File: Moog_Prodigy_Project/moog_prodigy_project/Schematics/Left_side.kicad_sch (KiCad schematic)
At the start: 70 parts, among them Q1 BC549, Q3 BC549, SW1 Switch_4x4, SW2 Switch_4x4, U2 NE5532, U2A1 OPA134, U2B1 OPA134, U3 NE5532, U4 NE5532, U5 LT1011CN8

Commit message: MOOG prodigy final 03.07.2026
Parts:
- R13: value 4K75 -> 4K75 1%
- R18: value 18K2 -> 18K2 1%
- R29: value 51M -> 51M 1%
- R3: value 63K4 -> 63K4 1%
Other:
- note added: "NAPOMENA 1 Kondenzatori: C37,C38,C39,C49,C41,C42, C43,C44,C45,C46,C47,C48 su vrednosti 100n i oni su kvalitetniji"
- note added: "NAPOMENA 2 Otpornici cija je vrednost: 63K4, 18K2, 4K75, 6K81, 51M, 2M4 su otpornici iz E96 serije (1%) Ostali orpotnici su iz serije E24 (5%)"
- note added: "Talasni oblik signala po promeni položaja preklopnika: Rampa - levi položaj Trougao - srednji položaj Četvrtke - desni položaj"
- note removed: "NAPOMENA Kondenzatori: C37,C38,C39,C49,C41,C42, C43,C44,C45,C46,C47,C48 su vrednosti 100n i oni su kvalitetniji"
- note removed: "Talasni oblik signala po promeni položaja preklopnika: Rampa - krajnji levi položaj Trougao - srednji položaj Četvrtke - krajnji desni položaj"
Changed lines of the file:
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@@
 		(comment 4 "Jovan Mastelica E1 105/2023")
 	)
+	(text "NAPOMENA 2\nOtpornici cija je vrednost:\n63K4, 18K2, 4K75, 6K81, 51M, 2M4\nsu otpornici iz E96 serije (1%)\nOstali orpotnici su iz serije E24 (5%)"
+		(exclude_from_sim no)
+		(at 217.678 160.02 0)
+		(effects
+			(font
+				(size 1.27 1.27)
+				(thickness 0.254)
+				(bold yes)
+			)
+			(justify left)
+		)
+	)
 	(text "OSC 1 CHIP \nTEMP TRIM"
 		(exclude_from_sim no)
@@
 		)
 	)
-	(text "Talasni oblik signala po promeni položaja preklopnika:\nRampa - krajnji levi položaj\nTrougao - srednji položaj\nČetvrtke - krajnji desni položaj\n"
+	(text "Talasni oblik signala po promeni položaja preklopnika:\nRampa -  levi položaj\nTrougao - srednji položaj\nČetvrtke - desni položaj\n"
 		(exclude_from_sim no)
-		(at 215.9 28.956 0)
+		(at 218.694 28.702 0)
 		(effects
 			(font
 				(size 1.27 1.27)
+				(thickness 0.254)
+				(bold yes)
 			)
 			(justify left)
@@
 		)
 	)
-	(text "NAPOMENA\nKondenzatori:\nC37,C38,C39,C49,C41,C42,\nC43,C44,C45,C46,C47,C48\nsu vrednosti 100n i oni su kvalitetniji"
+	(text "NAPOMENA 1\nKondenzatori:\nC37,C38,C39,C49,C41,C42,\nC43,C44,C45,C46,C47,C48\nsu vrednosti 100n i oni su kvalitetniji"
 		(exclude_from_sim no)
 		(at 177.038 160.274 0)
@@
 		(dnp no)
 		(property "Reference" "R3"
-			(at 28.702 153.162 0)
+			(at 27.178 152.908 0)
 			(effects
 				(font
@@
 			)
 		)
-		(property "Value" "63K4"
-			(at 27.432 155.448 0)
+		(property "Value" "63K4 1%"
+			(at 24.13 155.194 0)
 			(effects
 				(font
@@
 			)
 		)
-		(property "Value" "18K2"
+		(property "Value" "18K2 1%"
 			(at 147.574 125.73 0)
 			(effects
@@
 			)
 		)
-		(property "Value" "4K75"
+		(property "Value" "4K75 1%"
 			(at 109.474 68.834 90)
 			(effects
@@
 			)
 		)
-		(property "Value" "51M"
+		(property "Value" "51M 1%"
 			(at 251.46 134.874 90)
 			(effects

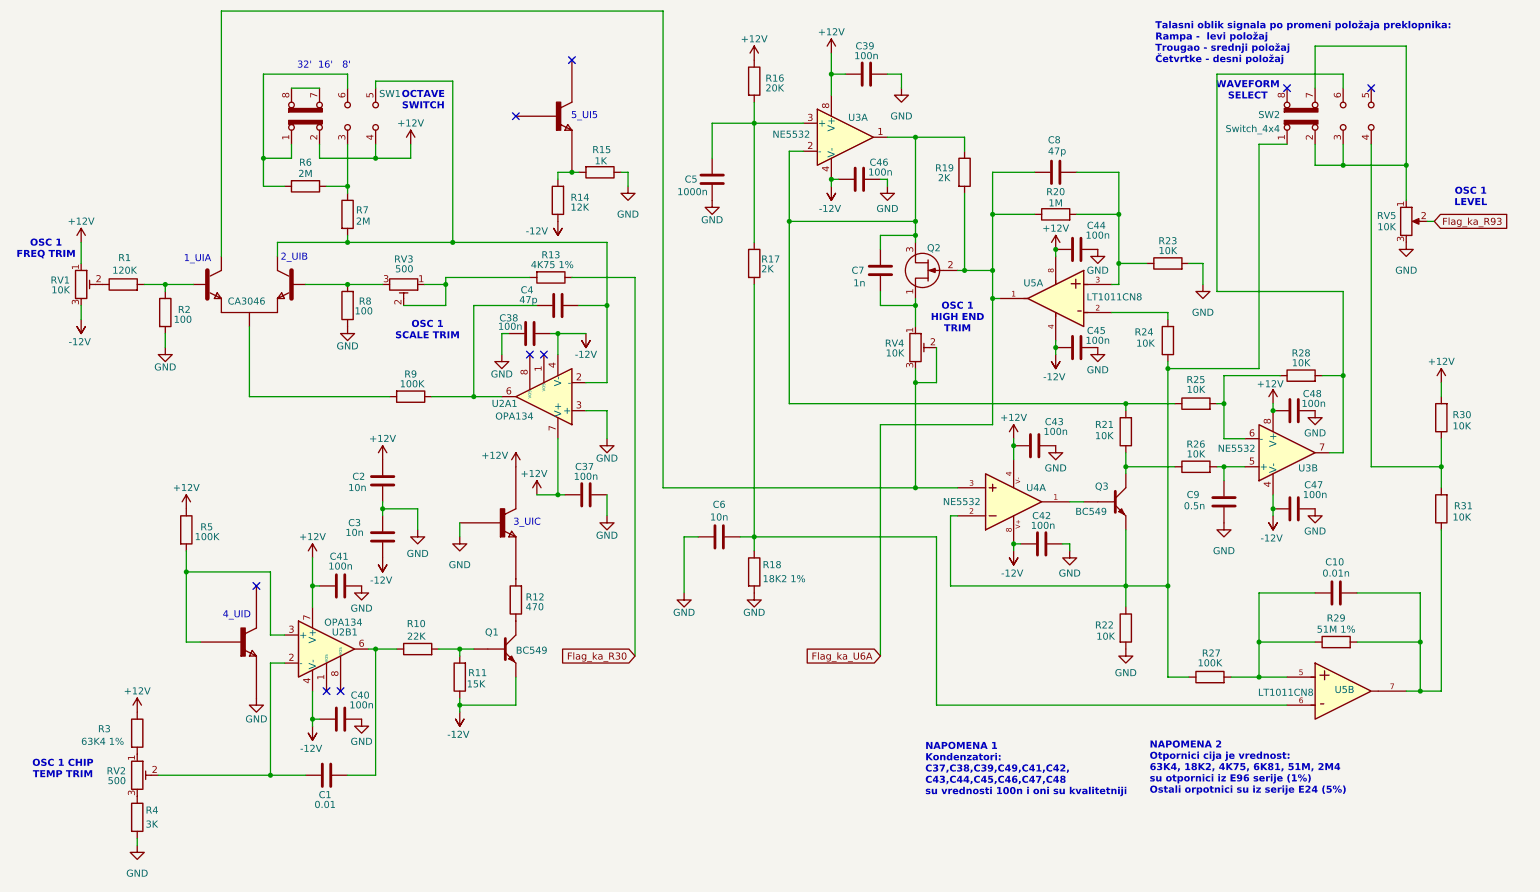
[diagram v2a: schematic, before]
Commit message: Moog prodigy fix 3
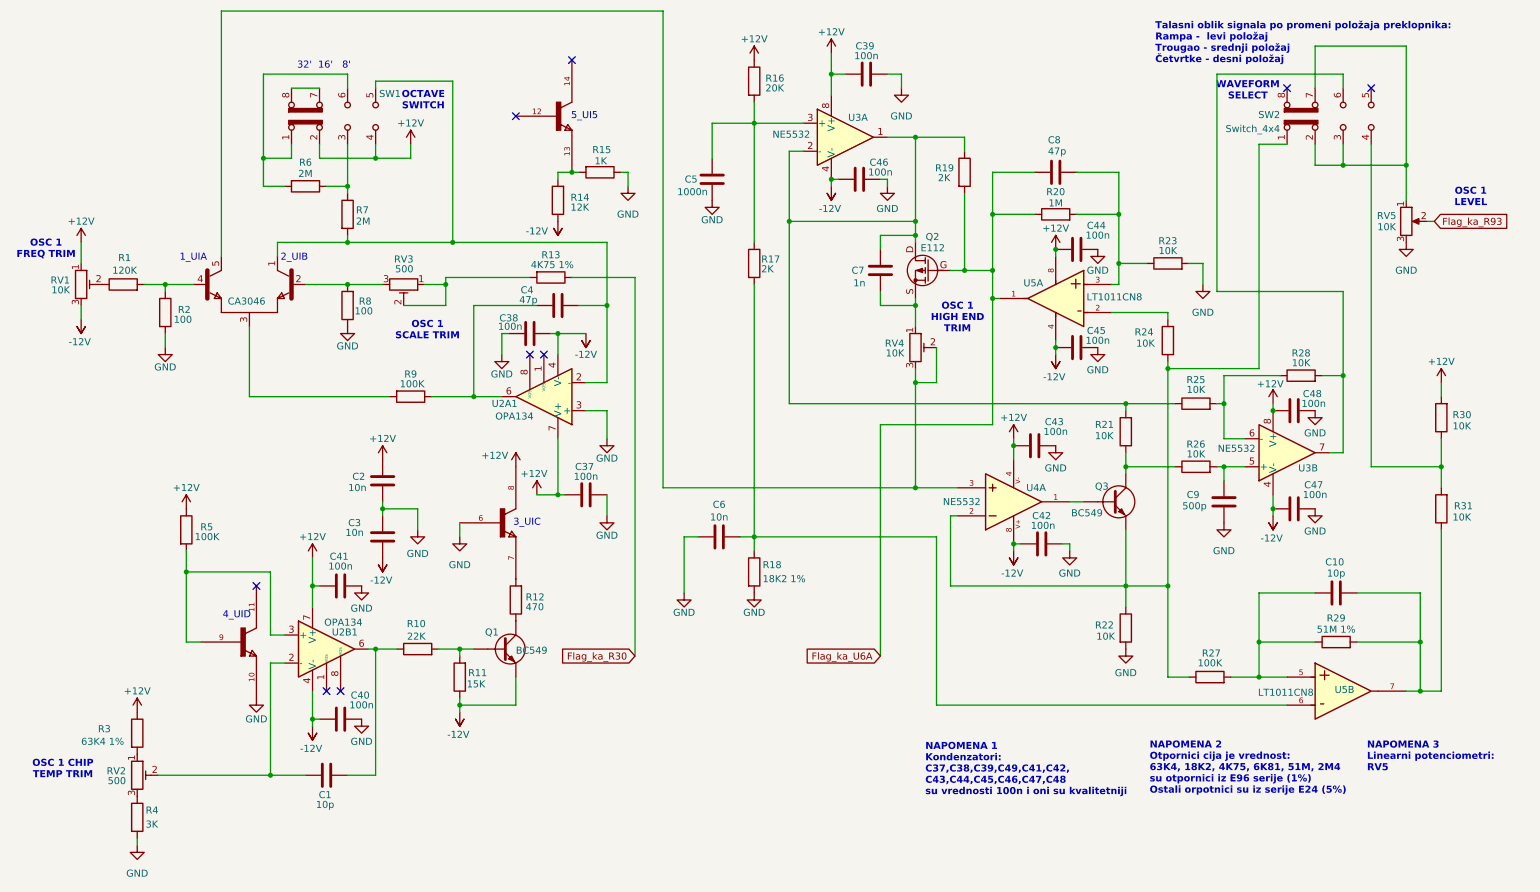
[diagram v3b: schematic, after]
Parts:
- C1: value 0.01 -> 10p
- C10: value 0.01n -> 10p
- C9: value 0.5n -> 500p
- Q2: value ~ -> E112
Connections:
- net +12V: now also CA3046.8; no longer CA3046.
- net Flag_ka_U6A: now also Q2.G; no longer Q2.2
- net GND: now also CA3046.10, CA3046.6; no longer CA3046.
- net at R1.2, R2.1: now also CA3046.4; no longer CA3046.
- net at C7.1, RV4.1: now also Q2.S; no longer Q2.1
- net at RV4.2, RV4.3, U4.3: now also CA3046.5; no longer CA3046.
- net at C4.2, R7.2, SW1.5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: now also CA3046.1; no longer CA3046.
- net at C7.2, R19.1, R21.2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: now also Q2.D; no longer Q2.3
- net at R8.2, RV3.3: now also CA3046.2; no longer CA3046.
- net at R12.2: now also CA3046.7; no longer CA3046.
- net at R9.2: now also CA3046.3; no longer CA3046.
- net at R14.2, R15.2: now also CA3046.13; no longer CA3046.
- net at R5.2, U2B1.3 (+): now also CA3046.9; no longer CA3046.
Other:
- note added: "NAPOMENA 3 Linearni potenciometri: RV5"
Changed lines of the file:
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@@
 		)
 	)
+	(text "NAPOMENA 3\nLinearni potenciometri:\nRV5"
+		(exclude_from_sim no)
+		(at 257.048 157.988 0)
+		(effects
+			(font
+				(size 1.27 1.27)
+				(thickness 0.254)
+				(bold yes)
+			)
+			(justify left)
+		)
+	)
 	(text "2_UIB"
 		(exclude_from_sim no)
@@
 	(text "1_UIA"
 		(exclude_from_sim no)
-		(at 45.212 67.818 0)
+		(at 44.45 67.564 0)
 		(effects
 			(font
@@
 	(wire
 		(pts
+			(xy 181.61 69.85) (xy 184.15 69.85)
+		)
+		(stroke
+			(width 0)
+			(type default)
+		)
+	)
+	(wire
+		(pts
 			(xy 78.74 111.76) (xy 78.74 113.03)
 		)
@@
 	(wire
 		(pts
-			(xy 182.88 69.85) (xy 184.15 69.85)
-		)
-		(stroke
-			(width 0)
-			(type default)
-		)
-	)
-	(wire
-		(pts
 			(xy 266.7 137.16) (xy 266.7 146.05)
 		)
@@
 	(symbol
 		(lib_id "Transistor_FET:BF256C")
-		(at 180.34 67.31 180)
+		(at 179.07 69.85 180)
 		(unit 1)
 		(exclude_from_sim no)
@@
 		(dnp no)
 		(property "Reference" "Q2"
-			(at 179.832 65.786 0)
+			(at 179.578 63.754 0)
 			(effects
 				(font
@@
 			)
 		)
-		(property "Value" "~"
-			(at 173.99 71.1199 0)
+		(property "Value" "E112"
+			(at 180.594 65.786 0)
 			(effects
 				(font
@@
 				)
 				(justify left)
-				(hide yes)
 			)
 		)
 		(property "Footprint" "Package_TO_SOT_THT:TO-92_Inline"
-			(at 180.34 67.31 0)
+			(at 179.07 69.85 0)
 			(effects
 				(font
@@
 		)
 		(property "Datasheet" ""
-			(at 180.34 67.31 0)
+			(at 179.07 69.85 0)
 			(effects
 				(font
@@
 		)
 		(property "Description" ""
-			(at 180.34 67.31 0)
+			(at 179.07 69.85 0)
 			(effects
 				(font
@@
 			)
 		)
-		(pin "1"
+		(pin "D"
 		)
-		(pin "3"
+		(pin "G"
 		)
-		(pin "2"
+		(pin "S"
 		)
 		(instances
@@
 			)
 		)
-		(property "Value" "0.01"
+		(property "Value" "10p"
 			(at 68.326 166.624 90)
 			(effects
@@
 			)
 		)
-		(pin ""
+		(pin "11"
 		)
-		(pin ""
+		(pin "10"
 		)
-		(pin ""
+		(pin "4"
 		)
-		(pin ""
+		(pin "2"
 		)
-		(pin ""
+		(pin "13"
 		)
-		(pin ""
+		(pin "7"
 		)
-		(pin ""
+		(pin "9"
 		)
-		(pin ""
+		(pin "5"
 		)
-		(pin ""
+		(pin "12"
 		)
-		(pin ""
+		(pin "14"
 		)
-		(pin ""
+		(pin "3"
 		)
-		(pin ""
+		(pin "8"
 		)
-		(pin ""
+		(pin "6"
 		)
-		(pin ""
+		(pin "1"
 		)
 		(instances
@@
 		)
 		(property "Value" "BC549"
-			(at 204.216 113.538 0)
+			(at 203.454 113.792 0)
 			(effects
 				(font
@@
 			)
 		)
-		(property "Value" "0.01n"
+		(property "Value" "10p"
 			(at 251.46 124.714 90)
 			(effects
@@
 			)
 		)
-		(property "Value" "0.5n"
+		(property "Value" "500p"
 			(at 225.806 112.522 0)
 			(effects

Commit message: treba mi da preraspodelim CA 3046
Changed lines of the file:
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@@
 	(text "OSC 1\nSCALE TRIM"
 		(exclude_from_sim no)
-		(at 86.868 80.772 0)
+		(at 84.328 80.264 0)
 		(effects
 			(font
@@
 	(text "OSC 1 \nHIGH END\nTRIM"
 		(exclude_from_sim no)
-		(at 182.88 78.486 0)
+		(at 181.864 80.518 0)
 		(effects
 			(font
@@
 		)
 		(property "Value" "BC549"
-			(at 102.87 138.684 0)
+			(at 103.632 141.986 0)
 			(effects
 				(font
@@
 		(dnp no)
 		(property "Reference" "U4"
-			(at 197.104 109.22 0)
+			(at 183.896 103.886 0)
 			(effects
 				(font
@@
 		)
 		(property "Value" "NE5532"
-			(at 183.642 111.76 0)
+			(at 183.642 106.426 0)
 			(effects
 				(font
@@
 		)
 		(property "Value" "BC549"
-			(at 203.454 113.792 0)
+			(at 206.502 115.824 0)
 			(effects
 				(font
@@
 		)
 		(property "Value" "LT1011CN8"
-			(at 247.396 146.304 0)
+			(at 262.636 150.368 0)
 			(effects
 				(font

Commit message: 04.07.2026 Dodati tolerancije, E94, prosiriti spisak
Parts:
- removed U4: NE5532, NE5532AP:DIP794W45P254L1016H508Q8, symbol AD8066ARM:AD8066ARM
- added U18: NE5532, symbol Amplifier_Operational:NE5532
- added U4: NE5532, OPA134PA:DIP794W45P254L959H508Q8, symbol Comparator:MCP6562
- renumbered RV5 to RV5_LIN
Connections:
- net +12V: now also U18.4
- net -12V: now also U18.8
- net at Q3. (E), R22.1, R24.1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: now also U4.3 (+)
- net at C8.2, R20.2, R23.1: now also U5.5 (+); no longer U5.3
- net at CA3046.5, RV4.2, RV4.3: now also U4.2 (-)
- net at R25.2, R28.1: now also U3.5 (+); no longer U3.6 (-)
- net at R24.2: now also U5.6 (-); no longer U5.2
- net at Q3. (E): now also U4.1
- net at C9.2, R26.2: now also U3.6 (-); no longer U3.5 (+)
- net Flag_ka_R30 renamed Flag_to_R30
- net Flag_ka_R93 renamed Flag_to_R93
- net Flag_ka_U6A renamed Flag_to_U6A
- no-connect marks 9 -> 5
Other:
- note added: "Signal waveform depending on switch position: Ramp - left position Triangle - center position Square - right position"
- note removed: "NAPOMENA 3 Linearni potenciometri: RV5"
- note removed: "Talasni oblik signala po promeni položaja preklopnika: Rampa - levi položaj Trougao - srednji položaj Četvrtke - desni položaj"
- moved on the sheet: C42, C44, C45, R27, R3, R4, RV2, RV5_LIN, U5A

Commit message: 07.06.2026 fix 3
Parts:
- added R116, R117: 2K, Resistor_THT:R_Axial_DIN0207_L6.3mm_D2.5mm_P7.62mm_Horizontal, symbol Device:R
- R1: value 120K -> 121K
- R10: value 22K -> 20K
- R14: value 12K -> 11K8
- R18: value 18K2 1% -> 18K2
- R29: value 51M 1% -> 5M1 1%
- R3: value 63K4 1% -> 63K4
- R4: value 3K -> 3K01
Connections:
- net at Q3. (E), R22.1, R24.1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: now also U4.2 (-); no longer U4.3 (+)
- net at CA3046.5, RV4.2, RV4.3: now also U4.3 (+); no longer U4.2 (-)
- net at CA3046.13, R15.2: now also R116.1; no longer R14.2
- new net: Q1. (E), R11.2, R117.2
- new net: R116.2, R14.2
- new net: R10.2, R117.1
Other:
- note removed: "NAPOMENA 2 Otpornici cija je vrednost: 63K4, 18K2, 4K75, 6K81, 51M, 2M4 su otpornici iz E96 serije (1%) Ostali orpotnici su iz serije E24 (5%)"
- moved on the sheet: C47, C48, C9, R10, R11, R14, R25, R26, R28, U3B, U3C

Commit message: CA3046 nova schema
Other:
- note added: "NAPOMENA 1 Kondenzatori: C2,C3,C37,C38,C39,C49,C41,C42, C43,C44,C45,C46,C47,C48 su vrednosti 100n i oni su kvalitetniji"
- note removed: "NAPOMENA 1 Kondenzatori: C37,C38,C39,C49,C41,C42, C43,C44,C45,C46,C47,C48 su vrednosti 100n i oni su kvalitetniji"
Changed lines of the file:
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@@
 		)
 	)
-	(text "NAPOMENA 1\nKondenzatori:\nC37,C38,C39,C49,C41,C42,\nC43,C44,C45,C46,C47,C48\nsu vrednosti 100n i oni su kvalitetniji"
+	(text "NAPOMENA 1\nKondenzatori:\nC2,C3,C37,C38,C39,C49,C41,C42,\nC43,C44,C45,C46,C47,C48\nsu vrednosti 100n i oni su kvalitetniji"
 		(exclude_from_sim no)
 		(at 177.038 160.274 0)
@@
 		)
 		(instances
-			(project ""
+			(project "moog_prodigy_project"
 				(path "/db469bdb-b6c3-4a16-9199-d4e6b8d556e8/6ca03b6b-5ad1-455d-b55d-f800979e8812"
 					(reference "U18")
